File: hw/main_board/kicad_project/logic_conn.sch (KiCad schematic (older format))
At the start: 10 parts, among them U8 MAX3002, U9 MAX3002

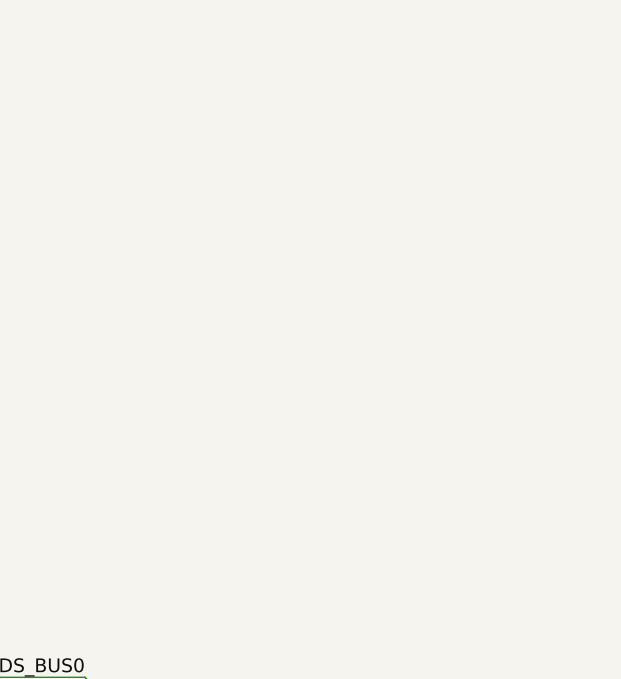
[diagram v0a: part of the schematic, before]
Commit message: PWR_board hierarchy added
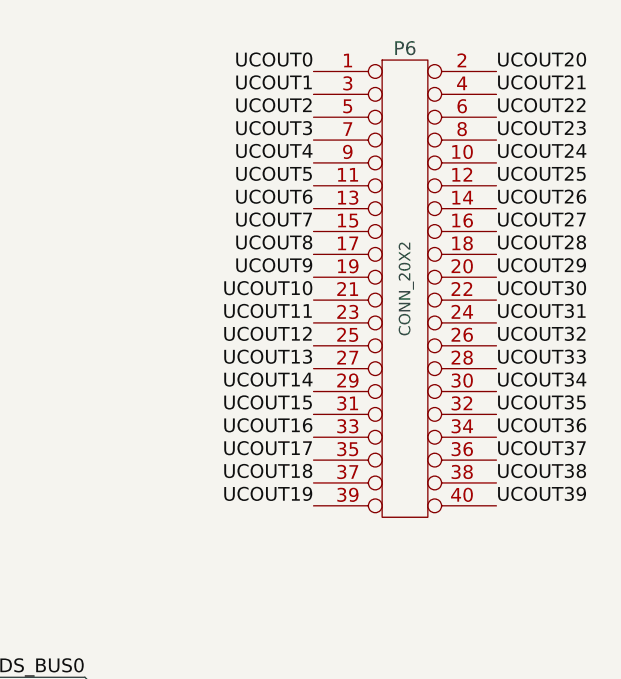
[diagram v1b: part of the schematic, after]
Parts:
- added P6: CONN_20X2, symbol CONN_20X2
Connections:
- net CLOCK_TWI0: now also P6.8 (P8)
- net CLOCK_TWI1: now also P6.10 (P10)
- net DDS_BUS0: now also P6.12 (P12)
- net DDS_BUS1: now also P6.14 (P14)
- net DDS_BUS2: now also P6.16 (P16)
- net DDS_BUS3: now also P6.18 (P18)
- net DDS_BUS4: now also P6.20 (P20)
- net DDS_BUS5: now also P6.22 (P22)
- net DDS_BUS6: now also P6.24 (P24)
- net GAIN_BUS0: now also P6.32 (P32)
- net GAIN_BUS1: now also P6.34 (P34)
- net GAIN_BUS2: now also P6.36 (P36)
- net GAIN_BUS3: now also P6.38 (P38)
- net GAIN_BUS4: now also P6.40 (P40)
- net IN_MUX0: now also P6.31 (P31)
- net IN_MUX1: now also P6.33 (P33)
- net IN_MUX2: now also P6.35 (P35)
- net IN_MUX3: now also P6.37 (P37)
- net OUT_MUX0: now also P6.39 (P39)
- net OUT_MUX1: now also P6.2 (P2)
- net OUT_MUX2: now also P6.4 (P4)
- net OUT_MUX3: now also P6.6 (P6)
- net RANGE_MUX0: now also P6.26 (P26)
- net RANGE_MUX1: now also P6.28 (P28)
- net RANGE_MUX2: now also P6.30 (P30)
- net UCOUT0: now also P6.1 (P1)
- net UCOUT1: now also P6.3 (P3)
- net UCOUT10: now also P6.21 (P21)
- net UCOUT11: now also P6.23 (P23)
- net UCOUT12: now also P6.25
- net UCOUT13: now also P6.27 (P27)
- net UCOUT14: now also P6.29 (P29)
- net UCOUT2: now also P6.5 (P5)
- net UCOUT3: now also P6.7 (P7)
- net UCOUT4: now also P6.9 (P9)
- net UCOUT5: now also P6.11 (P11)
- net UCOUT6: now also P6.13 (P13)
- net UCOUT7: now also P6.15 (P15)
- net UCOUT8: now also P6.17 (P17)
- net UCOUT9: now also P6.19 (P19)
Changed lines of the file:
@@
 LIBS:ddslib
 LIBS:demuxcomplib
-LIBS:noname-cache
-EELAYER 27 0
+LIBS:tDCS_driver-cache
+EELAYER 24 0
 EELAYER END
 $Descr A4 11693 8268
@@
 Sheet 3 3
 Title ""
-Date "5 oct 2013"
+Date "26 feb 2014"
 Rev ""
 Comp ""
@@
 Text HLabel 2200 2700 0    60   Input ~ 0
 MUXD[0...4]
+$Comp
+L CONN_20X2 P6
+U 1 1 530D6B88
+P 9050 1550
+F 0 "P6" H 9050 2600 60  0000 C CNN
+F 1 "CONN_20X2" V 9050 1550 50  0000 C CNN
+F 2 "" H 9050 1550 60  0000 C CNN
+F 3 "" H 9050 1550 60  0000 C CNN
+	1    9050 1550
+	1    0    0    -1
+$EndComp
+Text Label 8650 600  2    60   ~ 0
+UCOUT0
+Text Label 8650 700  2    60   ~ 0
+UCOUT1
+Text Label 8650 800  2    60   ~ 0
+UCOUT2
+Text Label 8650 900  2    60   ~ 0
+UCOUT3
+Text Label 8650 1000 2    60   ~ 0
+UCOUT4
+Text Label 8650 1100 2    60   ~ 0
+UCOUT5
+Text Label 8650 1200 2    60   ~ 0
+UCOUT6
+Text Label 8650 1300 2    60   ~ 0
+UCOUT7
+Text Label 8650 1400 2    60   ~ 0
+UCOUT8
+Text Label 8650 1500 2    60   ~ 0
+UCOUT9
+Text Label 8650 1600 2    60   ~ 0
+UCOUT10
+Text Label 8650 1700 2    60   ~ 0
+UCOUT11
+Text Label 8650 1800 2    60   ~ 0
+UCOUT12
+Text Label 8650 1900 2    60   ~ 0
+UCOUT13
+Text Label 8650 2000 2    60   ~ 0
+UCOUT14
+Text Label 8650 2100 2    60   ~ 0
+UCOUT15
+Text Label 8650 2200 2    60   ~ 0
+UCOUT16
+Text Label 8650 2300 2    60   ~ 0
+UCOUT17
+Text Label 8650 2400 2    60   ~ 0
+UCOUT18
+Text Label 8650 2500 2    60   ~ 0
+UCOUT19
+Text Label 9450 600  0    60   ~ 0
+UCOUT20
+Text Label 9450 700  0    60   ~ 0
+UCOUT21
+Text Label 9450 800  0    60   ~ 0
+UCOUT22
+Text Label 9450 900  0    60   ~ 0
+UCOUT23
+Text Label 9450 1000 0    60   ~ 0
+UCOUT24
+Text Label 9450 1100 0    60   ~ 0
+UCOUT25
+Text Label 9450 1200 0    60   ~ 0
+UCOUT26
+Text Label 9450 1300 0    60   ~ 0
+UCOUT27
+Text Label 9450 1400 0    60   ~ 0
+UCOUT28
+Text Label 9450 1500 0    60   ~ 0
+UCOUT29
+Text Label 9450 1600 0    60   ~ 0
+UCOUT30
+Text Label 9450 1700 0    60   ~ 0
+UCOUT31
+Text Label 9450 1800 0    60   ~ 0
+UCOUT32
+Text Label 9450 1900 0    60   ~ 0
+UCOUT33
+Text Label 9450 2000 0    60   ~ 0
+UCOUT34
+Text Label 9450 2100 0    60   ~ 0
+UCOUT35
+Text Label 9450 2200 0    60   ~ 0
+UCOUT36
+Text Label 9450 2300 0    60   ~ 0
+UCOUT37
+Text Label 9450 2400 0    60   ~ 0
+UCOUT38
+Text Label 9450 2500 0    60   ~ 0
+UCOUT39
 $EndSCHEMATC
